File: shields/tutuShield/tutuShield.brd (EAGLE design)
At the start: 22.8 x 22.9 mm, 6 parts

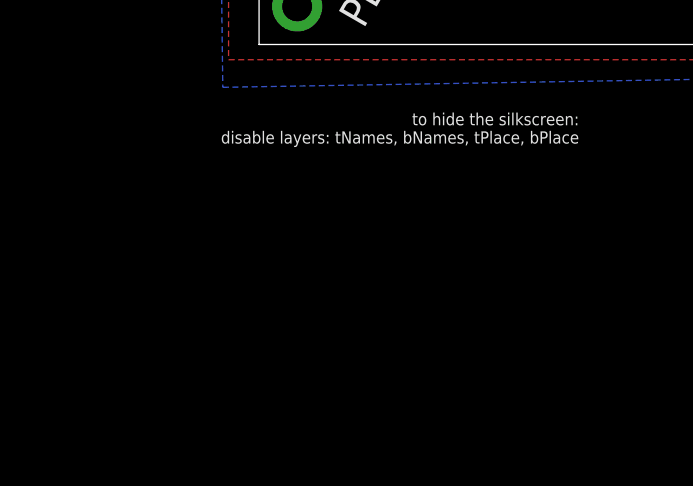
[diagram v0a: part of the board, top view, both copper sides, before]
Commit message: added MSGEQ7 to lib
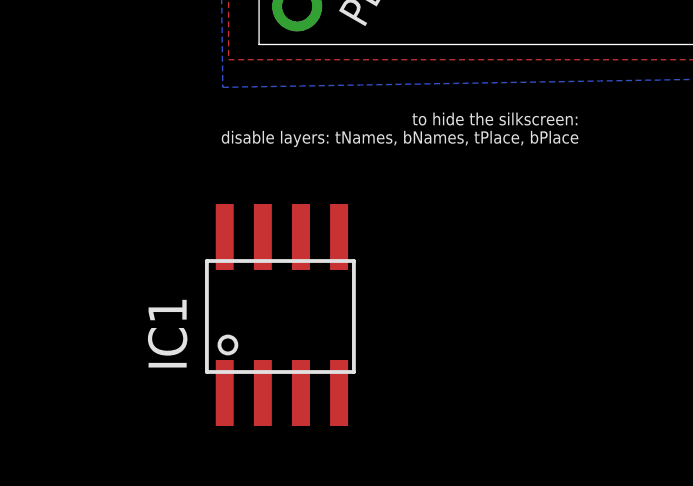
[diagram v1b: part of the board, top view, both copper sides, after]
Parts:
- added IC1: IC_MSGEQ7-SOIC8, ATtami:SOIC-8
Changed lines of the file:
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@@
 <layer number="20" name="Dimension" color="15" fill="1" visible="yes" active="yes"/>
 <layer number="21" name="tPlace" color="7" fill="1" visible="no" active="yes"/>
-<layer number="22" name="bPlace" color="7" fill="1" visible="yes" active="yes"/>
-<layer number="23" name="tOrigins" color="15" fill="1" visible="no" active="yes"/>
+<layer number="22" name="bPlace" color="7" fill="1" visible="no" active="yes"/>
+<layer number="23" name="tOrigins" color="15" fill="1" visible="yes" active="yes"/>
 <layer number="24" name="bOrigins" color="15" fill="1" visible="no" active="yes"/>
-<layer number="25" name="tNames" color="7" fill="1" visible="no" active="yes"/>
+<layer number="25" name="tNames" color="7" fill="1" visible="yes" active="yes"/>
 <layer number="26" name="bNames" color="7" fill="1" visible="yes" active="yes"/>
 <layer number="27" name="tValues" color="7" fill="1" visible="no" active="yes"/>
@@
 </element>
 <element name="U$3" library="ohw-logo" package="OSHW_6X150_NOTEXT" value="" x="10.668" y="7.112" rot="R90"/>
+<element name="IC1" library="ATtami" package="SOIC-8" value="IC_MSGEQ7-SOIC8" x="0.762" y="-9.017"/>
 </elements>
 <signals>

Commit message: didn't save last time :\
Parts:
- added C1: 33pF, ATtami:0805
- added C2, C4: 0.1uF, ATtami:0805
- added C3: 1000pF, ATtami:0805
- added JP1: (no value), ATtami:1X02_ROUND
- added R1: 200K, ATtami:0805
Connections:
- new net CKIN: C1.1, IC1.8, R1.1
- new net IN: C3.1, IC1.5
- new net N$1: C3.2, JP1.2
- new net N$4: IC1.6, JP1.1
- new net N$5: C2.1, IC1.2
- net GND: now also C1.2, C2.2, C4.1
- net PB0: now also IC1.7
- net PB1: now also IC1.4
- net PB2: now also IC1.3
- net VCC: now also C4.2, R1.2
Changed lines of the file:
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@@
 <?xml version="1.0" encoding="utf-8"?>
 <!DOCTYPE eagle SYSTEM "eagle.dtd">
-<eagle version="7.1.0">
+<eagle version="7.2.0">
 <drawing>
 <settings>
@@
 <element name="U$3" library="ohw-logo" package="OSHW_6X150_NOTEXT" value="" x="10.668" y="7.112" rot="R90"/>
 <element name="IC1" library="ATtami" package="SOIC-8" value="IC_MSGEQ7-SOIC8" x="0.762" y="-9.017"/>
+<element name="C1" library="ATtami" package="0805" value="33pF" x="-5.588" y="-10.795"/>
+<element name="C2" library="ATtami" package="0805" value="0.1uF" x="-8.382" y="-10.795"/>
+<element name="C3" library="ATtami" package="0805" value="1000pF" x="-11.176" y="-10.795"/>
+<element name="C4" library="ATtami" package="0805" value="0.1uF" x="-13.97" y="-10.795"/>
+<element name="JP1" library="ATtami" package="1X02_ROUND" value="" x="-17.907" y="-9.017"/>
+<element name="R1" library="ATtami" package="0805" value="200K" x="-22.479" y="-10.795"/>
 </elements>
 <signals>
@@
 <contactref element="J2" pad="2"/>
 <contactref element="J1" pad="1"/>
+<contactref element="C4" pad="1"/>
+<contactref element="C2" pad="2"/>
+<contactref element="C1" pad="2"/>
 <wire x1="21.59" y1="1.27" x2="21.59" y2="11.43" width="0" layer="19" extent="1-1"/>
 <wire x1="1.27" y1="16.51" x2="21.59" y2="11.43" width="0" layer="19" extent="1-1"/>
+<wire x1="-4.688" y1="-10.795" x2="1.27" y2="16.51" width="0" layer="19" extent="1-1"/>
+<wire x1="-7.482" y1="-10.795" x2="-4.688" y2="-10.795" width="0" layer="19" extent="1-1"/>
+<wire x1="-14.87" y1="-10.795" x2="-7.482" y2="-10.795" width="0" layer="19" extent="1-1"/>
 </signal>
 <signal name="VCC">
 <contactref element="J3" pad="1"/>
+<contactref element="C4" pad="2"/>
+<contactref element="R1" pad="2"/>
+<wire x1="-13.07" y1="-10.795" x2="-21.579" y2="-10.795" width="0" layer="19" extent="1-1"/>
+<wire x1="21.59" y1="3.81" x2="-13.07" y2="-10.795" width="0" layer="19" extent="1-1"/>
 </signal>
 <signal name="N$2">
@@
 <signal name="PB0">
 <contactref element="J1" pad="2"/>
+<contactref element="IC1" pad="7"/>
+<wire x1="0.127" y1="-6.417" x2="1.27" y2="13.97" width="0" layer="19" extent="1-1"/>
 </signal>
 <signal name="PB1">
 <contactref element="J1" pad="3"/>
+<contactref element="IC1" pad="4"/>
+<wire x1="2.667" y1="-11.617" x2="1.27" y2="11.43" width="0" layer="19" extent="1-1"/>
 </signal>
 <signal name="PB2">
 <contactref element="J1" pad="4"/>
+<contactref element="IC1" pad="3"/>
+<wire x1="1.27" y1="8.89" x2="1.397" y2="-11.617" width="0" layer="19" extent="1-1"/>
 </signal>
 <signal name="PB3">
@@
 <contactref element="J1" pad="7"/>
 </signal>
+<signal name="IN">
+<contactref element="IC1" pad="5"/>
+<contactref element="C3" pad="1"/>
+<wire x1="2.667" y1="-6.417" x2="-12.076" y2="-10.795" width="0" layer="19" extent="1-1"/>
+</signal>
+<signal name="N$1">
+<contactref element="C3" pad="2"/>
+<contactref element="JP1" pad="2"/>
+<wire x1="-10.276" y1="-10.795" x2="-16.637" y2="-9.017" width="0" layer="19" extent="1-1"/>
+</signal>
+<signal name="N$4">
+<contactref element="IC1" pad="6"/>
+<contactref element="JP1" pad="1"/>
+<wire x1="1.397" y1="-6.417" x2="-19.177" y2="-9.017" width="0" layer="19" extent="1-1"/>
+</signal>
+<signal name="N$5">
+<contactref element="C2" pad="1"/>
+<contactref element="IC1" pad="2"/>
+<wire x1="0.127" y1="-11.617" x2="-9.282" y2="-10.795" width="0" layer="19" extent="1-1"/>
+</signal>
+<signal name="CKIN">
+<contactref element="IC1" pad="8"/>
+<contactref element="C1" pad="1"/>
+<contactref element="R1" pad="1"/>
+<wire x1="-6.488" y1="-10.795" x2="-23.379" y2="-10.795" width="0" layer="19" extent="1-1"/>
+<wire x1="-1.143" y1="-6.417" x2="-6.488" y2="-10.795" width="0" layer="19" extent="1-1"/>
+</signal>
 </signals>

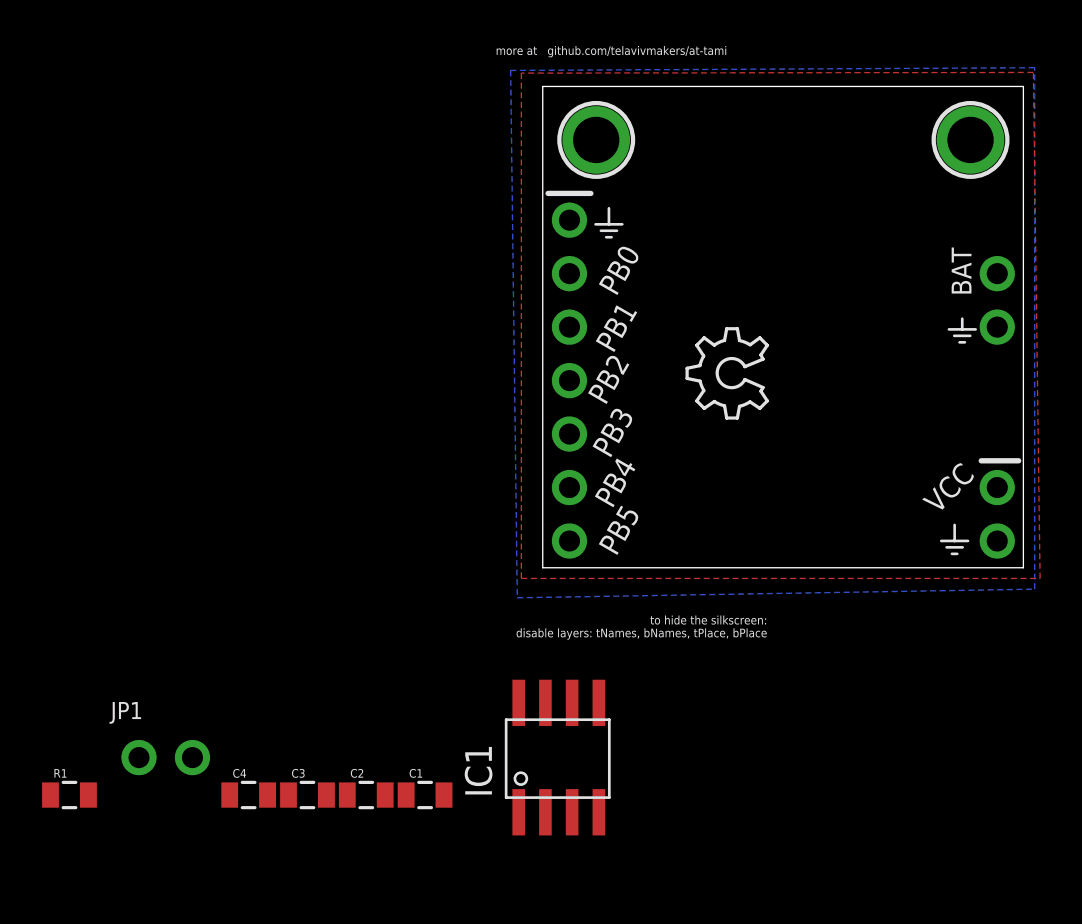
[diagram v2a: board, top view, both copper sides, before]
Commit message: added the pb5 as digitall/reset pin thing
also text comments
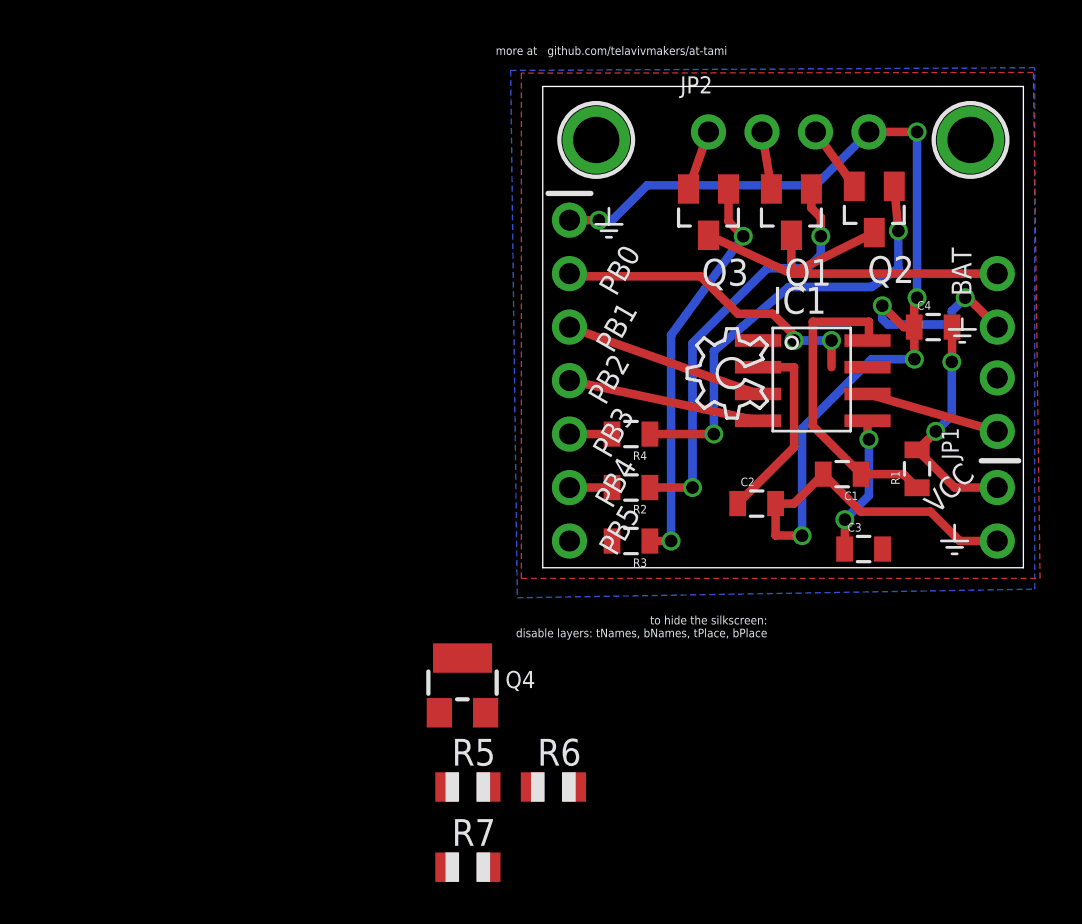
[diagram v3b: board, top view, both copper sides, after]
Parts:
- added JP2: (no value), ATtami:1X04_ROUND
- added Q1, Q2, Q3: (no value), dp_devices:SOT-23
- added Q4: 2N3904, microbuilder:SOT23-W
- added R2, R3, R4: 10K, ATtami:0805
- added R5, R6, R7: 1k, adafruit:R0805
- moved R1 43.1 mm to (17.8, 4.70), turned to 90 degrees
- moved JP1 42.9 mm to (21.6, 7.75), turned to 90 degrees
- moved C4 39.4 mm to (18.5, 11.4)
- moved C3 28.9 mm to (15.2, 0.89)
- moved C1 25.0 mm to (14.2, 4.45), turned to 180 degrees
- moved C2 23.1 mm to (10.2, 3.05)
- moved IC1 21.6 mm to (12.8, 8.89), turned to 270 degrees
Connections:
- removed net N$1: C3.2, JP1.2
- new net $$$: IC1.7, R6.1
- new net N$10: JP2.3, Q2.2
- new net N$11: JP2.2, Q1.2
- new net N$13: JP2.1, Q3.2
- new net N$14: Q4.1, R6.2
- new net N$6: Q1.1, R2.1
- new net N$7: Q2.1, R4.1
- new net N$8: Q4.2, R7.2
- new net V_BAT: J2.1, Q1.3, Q2.3, Q3.3
- net GND: now also JP2.4, R7.1
- net N$3: now also Q3.1, R3.1; no longer J2.1
- net PB0: now also R3.2; no longer IC1.7
- net PB1: now also IC1.3; no longer IC1.4
- net PB2: now also IC1.4; no longer IC1.3
- net PB3: now also R4.2
- net PB4: now also R2.2
- net PB5: now also Q4.3, R5.2
- net VCC: now also C3.2, JP1.2, R5.1
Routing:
- net GND: track 0.00 -> 66.1 mm, vias 0 -> 7
- net N$7: track 0.00 -> 21.0 mm, vias 0 -> 2
- net V_BAT: track 0.00 -> 20.3 mm
- net N$6: track 0.00 -> 20.0 mm, vias 0 -> 2
- net N$3: track 0.00 -> 19.1 mm, vias 0 -> 2
- net PB0: track 0.00 -> 15.2 mm, vias 0 -> 2
- net CKIN: track 0.00 -> 14.7 mm
- net VCC: track 0.00 -> 11.1 mm, vias 0 -> 2
- net PB1: track 0.00 -> 9.50 mm
- net N$5: track 0.00 -> 9.30 mm
- net PB2: track 0.00 -> 9.16 mm
- net IN: track 0.00 -> 6.60 mm, vias 0 -> 2
- net N$4: track 0.00 -> 6.41 mm
- net N$10: track 0.00 -> 3.17 mm
- net N$13: track 0.00 -> 2.87 mm
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
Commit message: sorry, i mixed signals
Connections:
- removed net $$$: IC1.7, R6.1
- net PB1: now also IC1.7, R6.1
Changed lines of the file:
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@@
 <contactref element="IC1" pad="3"/>
 <wire x1="1.27" y1="11.43" x2="10.227" y2="8.255" width="0.4064" layer="1"/>
+<contactref element="R6" pad="1"/>
+<contactref element="IC1" pad="7"/>
+<wire x1="10.227" y1="8.255" x2="15.427" y2="9.525" width="0" layer="19" extent="1-1"/>
+<wire x1="-0.492" y1="-10.414" x2="10.227" y2="8.255" width="0" layer="19" extent="1-1"/>
 </signal>
 <signal name="PB2">
@@
 <wire x1="-4.91" y1="-6.888" x2="1.508" y2="-10.414" width="0" layer="19" extent="1-1"/>
 </signal>
-<signal name="$$$">
-<contactref element="R6" pad="1"/>
-<contactref element="IC1" pad="7"/>
-<wire x1="-0.492" y1="-10.414" x2="15.427" y2="9.525" width="0" layer="19" extent="1-1"/>
-</signal>
 </signals>

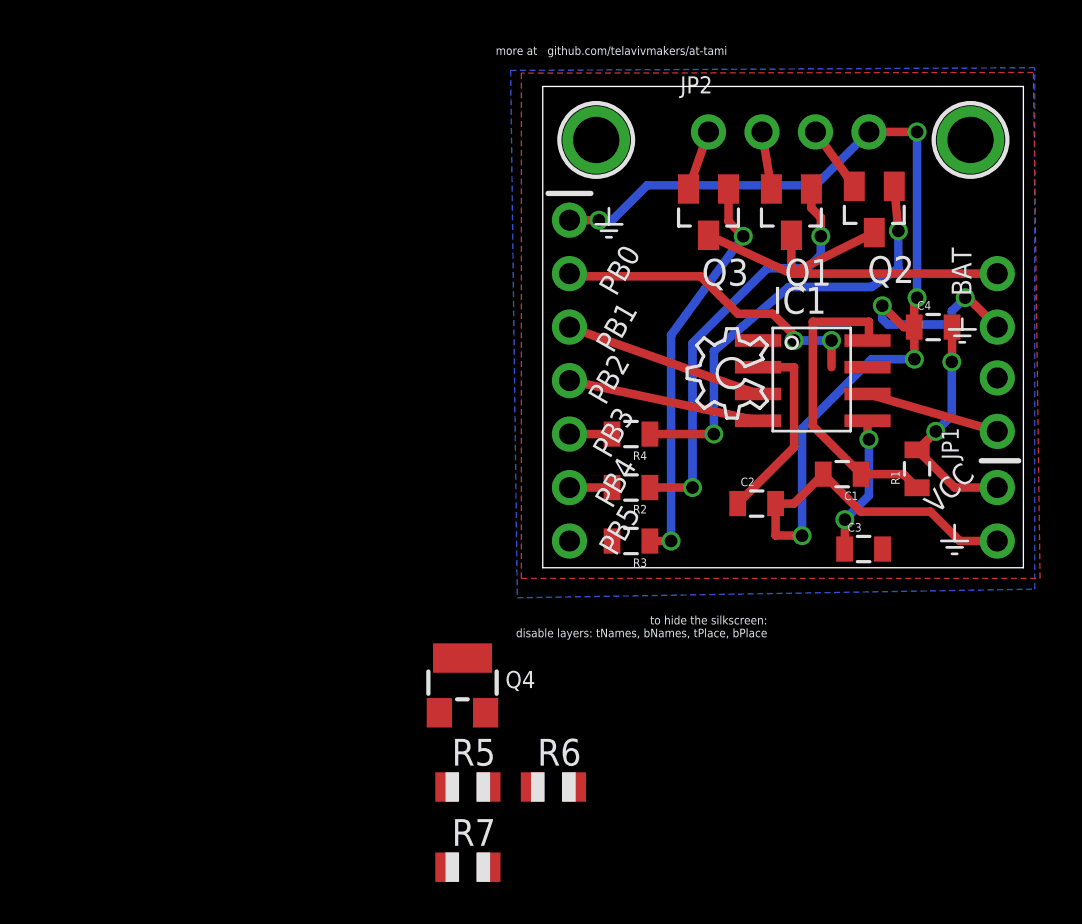
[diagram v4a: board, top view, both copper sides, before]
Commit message: a version without the PB5 trick
it might be a bit simpler but i think its worth it to stick to
4af68e7c457e82ac5364ccc3b228164f2045e11b
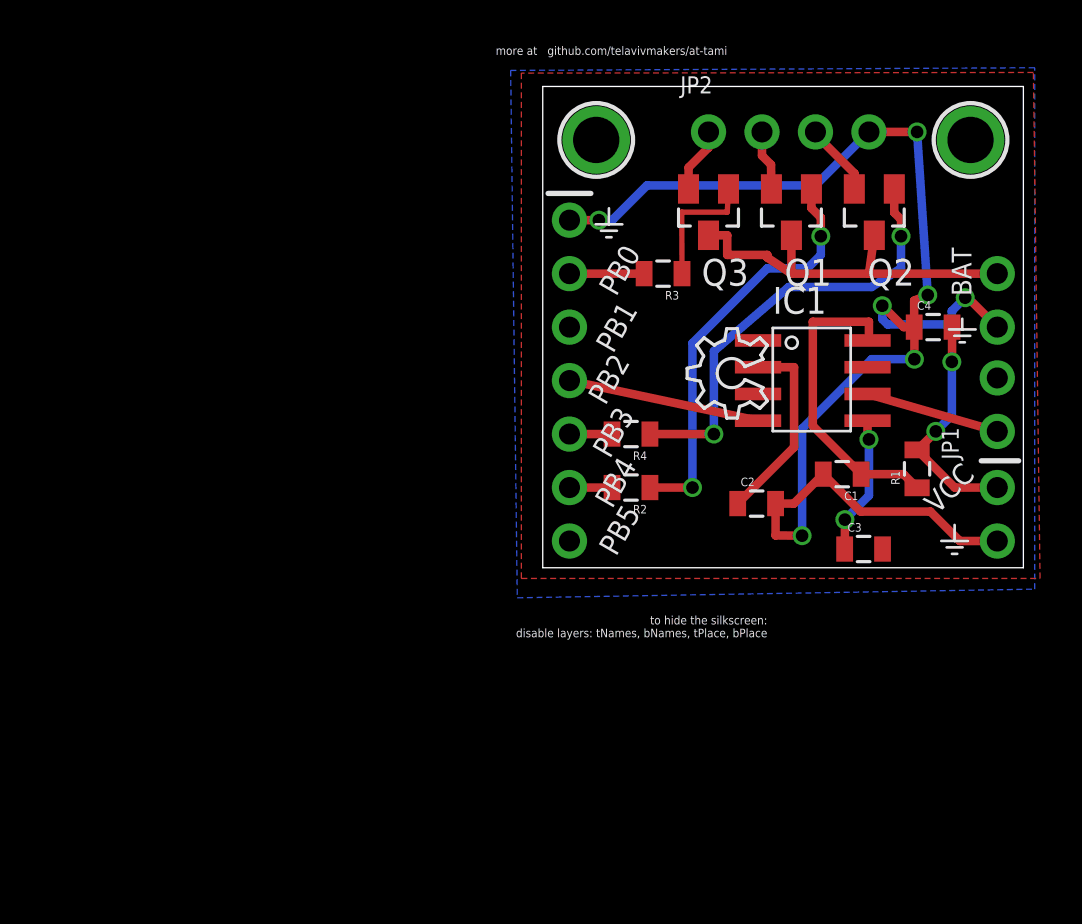
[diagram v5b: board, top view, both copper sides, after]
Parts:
- removed Q4: 2N3904, microbuilder:SOT23-W
- removed R5, R6, R7: 1k, adafruit:R0805
- moved R3 12.8 mm to (5.71, 14.0)
- moved Q2 0.13 mm to (15.7, 16.9)
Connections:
- removed net N$14: Q4.1, R6.2
- removed net N$8: Q4.2, R7.2
- net GND: no longer R7.1
- net PB1: no longer IC1.3, R6.1
- net PB5: now also IC1.3; no longer Q4.3, R5.2
- net VCC: no longer R5.1
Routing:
- net N$3: track 19.1 -> 6.18 mm, vias 2 -> 0
- net PB0: track 15.2 -> 3.55 mm, vias 2 -> 0
- net PB1: track 9.50 -> 0.00 mm
- net V_BAT: track 20.3 -> 18.7 mm
